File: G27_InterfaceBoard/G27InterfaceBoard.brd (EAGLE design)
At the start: 60 x 60 mm, 32 parts, among them IC1 LMV321M5, IC2 74HC126D, J1 Pedal, J2 Shifter, U1 LMV324

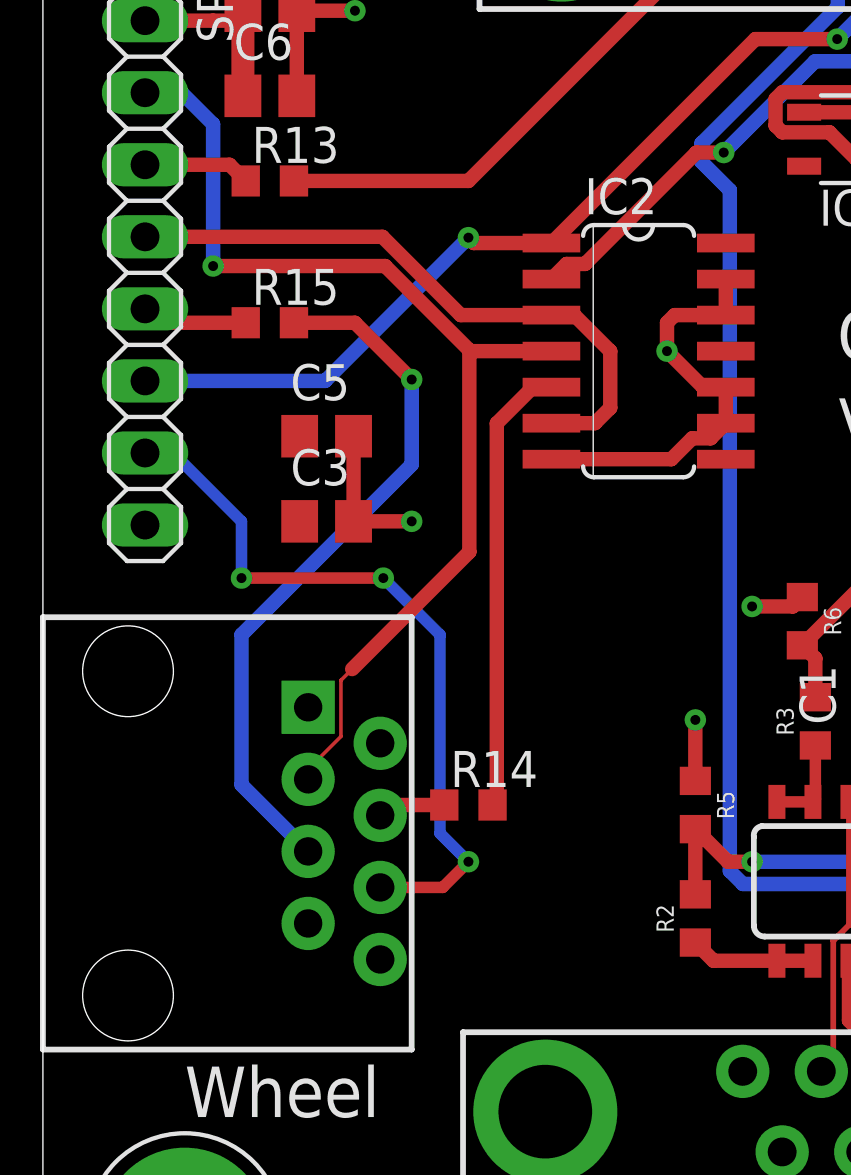
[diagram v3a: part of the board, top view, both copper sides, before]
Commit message: Add missing trace for wheel SCK.
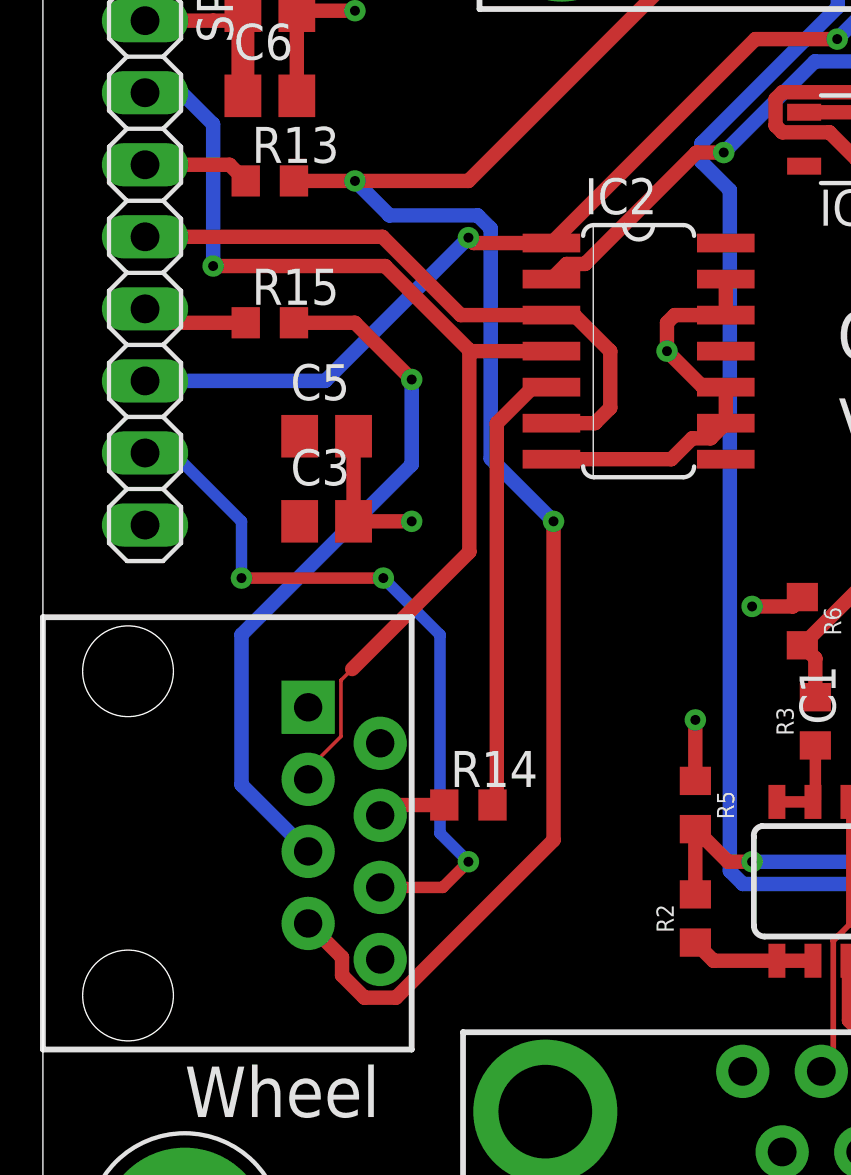
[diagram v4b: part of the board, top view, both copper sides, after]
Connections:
- removed net SCLK: WHEEL.7
- net SCK: now also WHEEL.7
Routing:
- net SCK: track 32.1 -> 72.4 mm, vias 1 -> 3
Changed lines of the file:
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@@
 <contactref element="J2" pad="1"/>
 <contactref element="R13" pad="2"/>
-<wire x1="8.85" y1="-18" x2="15" y2="-18" width="0.508" layer="1"/>
+<wire x1="8.85" y1="-18" x2="11" y2="-18" width="0.508" layer="1"/>
+<wire x1="11" y1="-18" x2="15" y2="-18" width="0.508" layer="1"/>
 <wire x1="22" y1="-11" x2="15" y2="-18" width="0.508" layer="1"/>
 <via x="22" y="-11" extent="1-16" drill="0.35"/>
@@
 <wire x1="34.11761875" y1="-9.2138" x2="35.46381875" y2="-10.56" width="0.508" layer="16"/>
 <wire x1="23.1418625" y1="-9.2138" x2="34.11761875" y2="-9.2138" width="0.508" layer="16"/>
+<contactref element="WHEEL" pad="7"/>
+<wire x1="10.5438" y1="-46.00261875" x2="11.33238125" y2="-46.7912" width="0.508" layer="1"/>
+<wire x1="11.33238125" y1="-46.7912" x2="12.44761875" y2="-46.7912" width="0.508" layer="1"/>
+<wire x1="9.35" y1="-44.175" x2="10.5438" y2="-45.3688" width="0.508" layer="1"/>
+<wire x1="10.5438" y1="-45.3688" x2="10.5438" y2="-46.00261875" width="0.508" layer="1"/>
+<wire x1="12.44761875" y1="-46.7912" x2="18" y2="-41.23881875" width="0.508" layer="1"/>
+<wire x1="18" y1="-41.23881875" x2="18" y2="-30" width="0.508" layer="1"/>
+<via x="18" y="-30" extent="1-16" drill="0.35"/>
+<wire x1="15.7846" y1="-19.67500625" x2="15.32499375" y2="-19.2154" width="0.508" layer="16"/>
+<wire x1="12.2154" y1="-19.2154" x2="11" y2="-18" width="0.508" layer="16"/>
+<wire x1="15.32499375" y1="-19.2154" x2="12.2154" y2="-19.2154" width="0.508" layer="16"/>
+<wire x1="18" y1="-30" x2="15.7846" y2="-27.7846" width="0.508" layer="16"/>
+<wire x1="15.7846" y1="-27.7846" x2="15.7846" y2="-19.67500625" width="0.508" layer="16"/>
+<via x="11" y="-18" extent="1-16" drill="0.35"/>
 </signal>
 <signal name="MISO">
@@
 <wire x1="29.46921875" y1="-13.7846" x2="32.69381875" y2="-10.56" width="0.508" layer="16"/>
 </signal>
-<signal name="SCLK">
-<contactref element="WHEEL" pad="7"/>
-</signal>
 <signal name="N$9">
